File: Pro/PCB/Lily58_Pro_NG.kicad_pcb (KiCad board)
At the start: 2 copper layers, 142.5 x 106.3 mm, 87 parts, among them J1 LED, J2 4PIN, J3 OLED, P1 i2c_pin, P2 i2c_pin, SW1 SW_PUSH, SW10 SW_PUSH, SW11 SW_PUSH, SW12 SW_PUSH, SW13 SW_PUSH, SW14 SW_PUSH, SW15 SW_PUSH, SW16 SW_PUSH, SW17 SW_PUSH, SW18 SW_PUSH, SW19 SW_PUSH, SW2 SW_PUSH, SW20 SW_PUSH, SW21 SW_PUSH, SW22 SW_PUSH, SW23 SW_PUSH, SW24 SW_PUSH, SW25 SW_PUSH, SW26 SW_PUSH, SW27 SW_PUSH, SW28 SW_PUSH, SW29 SW_PUSH, SW3 SW_PUSH, SW30 SW_PUSH, SW31 Rotary_Encoder_Switch, SW4 SW_PUSH, SW5 SW_PUSH, SW6 SW_PUSH, SW7 SW_PUSH, SW8 SW_PUSH, SW9 SW_PUSH, U1 ProMicro

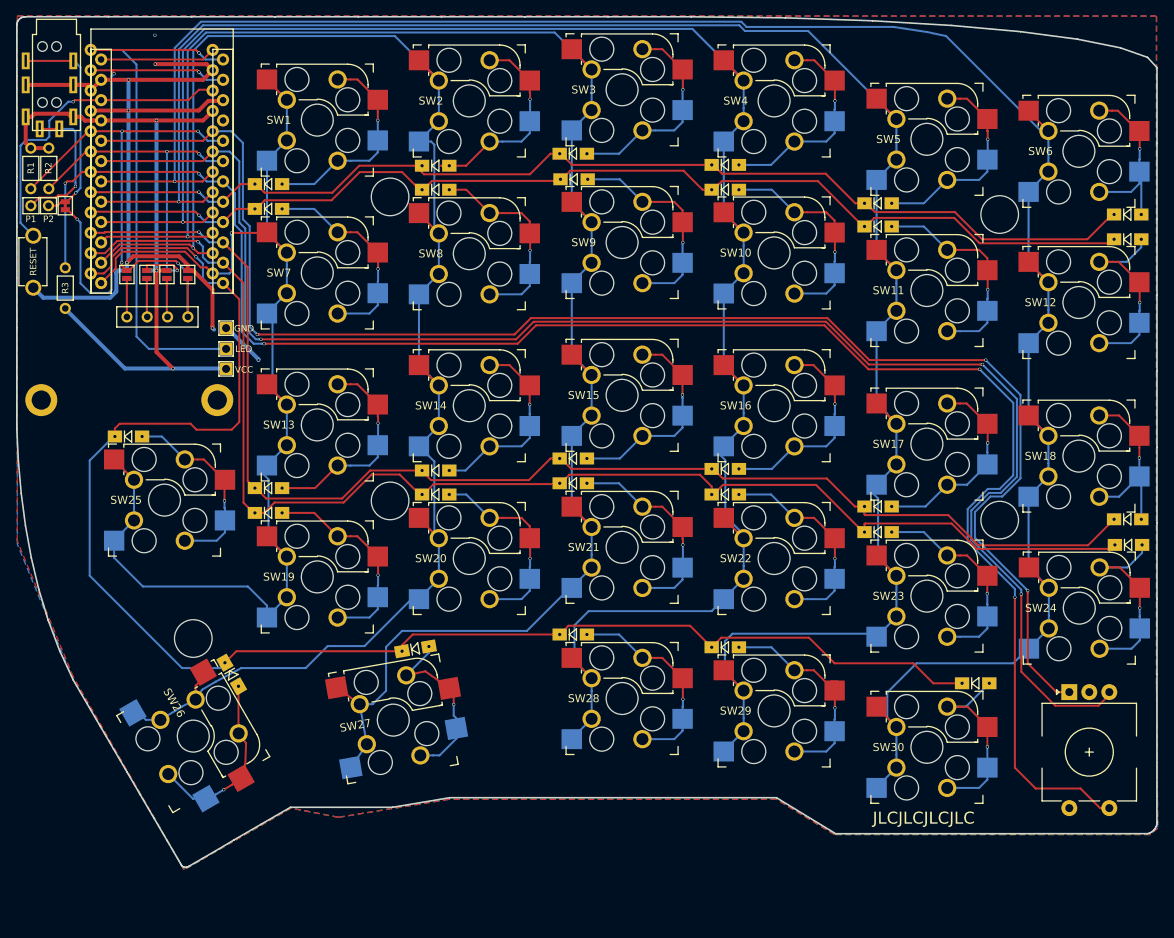
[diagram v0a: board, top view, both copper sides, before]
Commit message: Final version of Lily60 Evo PCB and Case
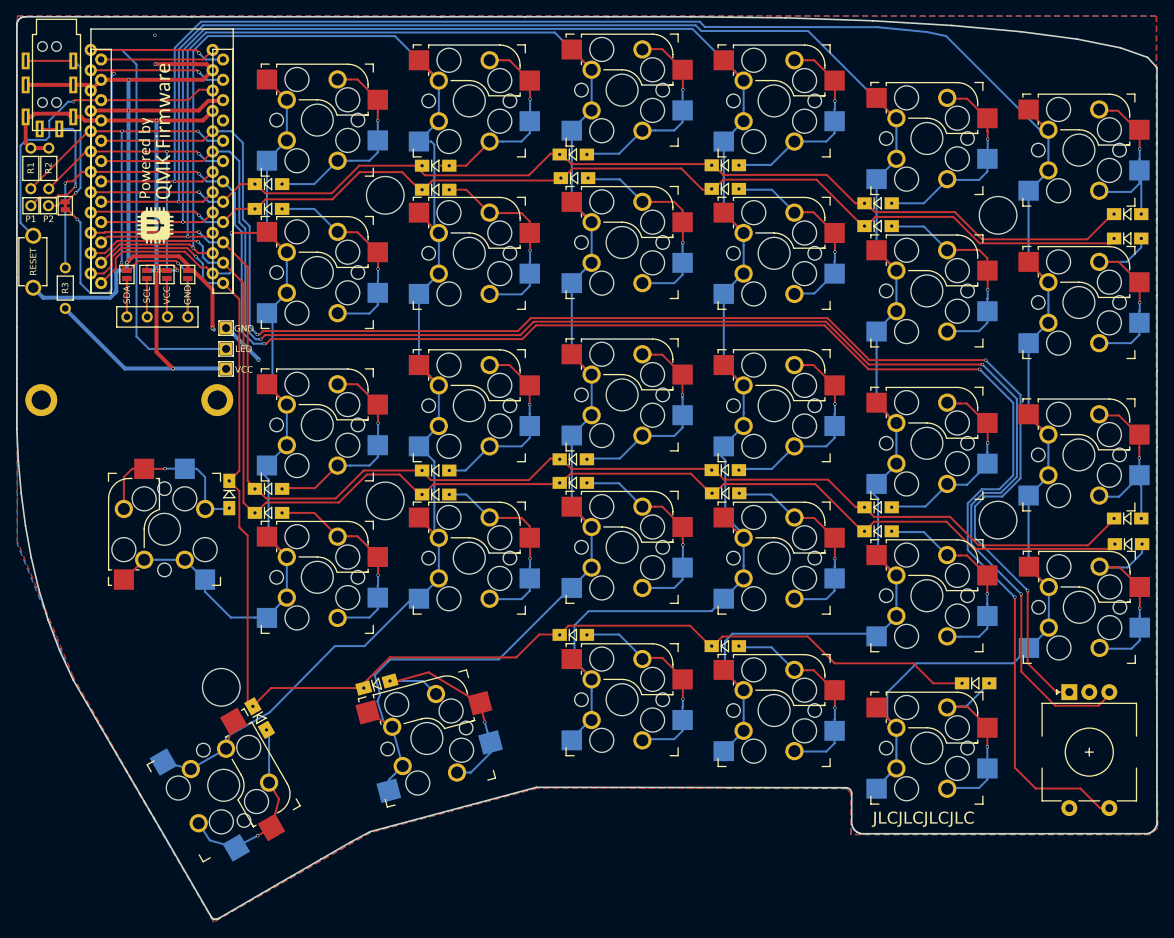
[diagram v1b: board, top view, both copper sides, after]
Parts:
- added G***: LOGO, Lily58_Pro-footprint:qmk-badge, B.Cu at (100.2, 54.1)
- added G***: LOGO, Lily58_Pro-footprint:qmk-badge, F.Cu at (100.2, 54.1)
- SW1, SW10, SW11, SW12, SW13, SW14, SW15, SW16, SW17, SW18, SW19, SW2, SW20, SW21, SW22, SW23, SW24, SW25, SW26, SW27, SW28, SW29, SW3, SW30, SW4, SW5, SW6, SW7, SW8, SW9: moved to B.Cu
- moved D25 14.5 mm to (109.5, 96.8), turned to 270 degrees
- moved SW26 7.23 mm to (108.8, 133.2)
- moved TH7 7.03 mm to (108.5, 120.9)
- moved D27 6.57 mm to (128.0, 120.5), turned to 15 degrees
- moved D26 6.48 mm to (113.3, 124.8)
- moved SW27 4.86 mm to (134.2, 127.3), turned to 15 degrees
- moved SW25 3.65 mm to (101.4, 101.2), turned to 90 degrees
- moved TH3 0.63 mm to (129.0, 59.4)
- moved TH5 0.60 mm to (129.0, 97.6)
- moved TH4 0.22 mm to (205.6, 61.9)
- moved TH6 0.20 mm to (205.6, 100.0)
- moved D9 0.16 mm to (152.7, 57.2)
- moved D22 0.16 mm to (171.6, 96.7)
- moved D16 0.15 mm to (171.5, 93.8)
- moved D29 0.15 mm to (171.5, 115.8)
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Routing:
- net row4: track 196.4 -> 174.2 mm
- net col5: track 155.0 -> 140.4 mm
- net Net-(D27-Pad2): track 22.9 -> 30.5 mm
- net Net-(D25-Pad2): track 26.2 -> 22.1 mm
- net Net-(D10-Pad2): track 28.7 -> 26.9 mm
- net col4: track 207.2 -> 205.6 mm
- net col3: track 225.3 -> 226.4 mm
- net row3: track 170.5 -> 169.8 mm
- net row2: track 167.0 -> 166.4 mm
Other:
- board size 142.5 x 106.3 mm -> 142.5 x 112.8 mm
- board text added: "GND"
- board text added: "SCL"
- board text added: "SDA"
- board text added: "VCC"

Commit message: SW31 can be an encoder or a MW Switch
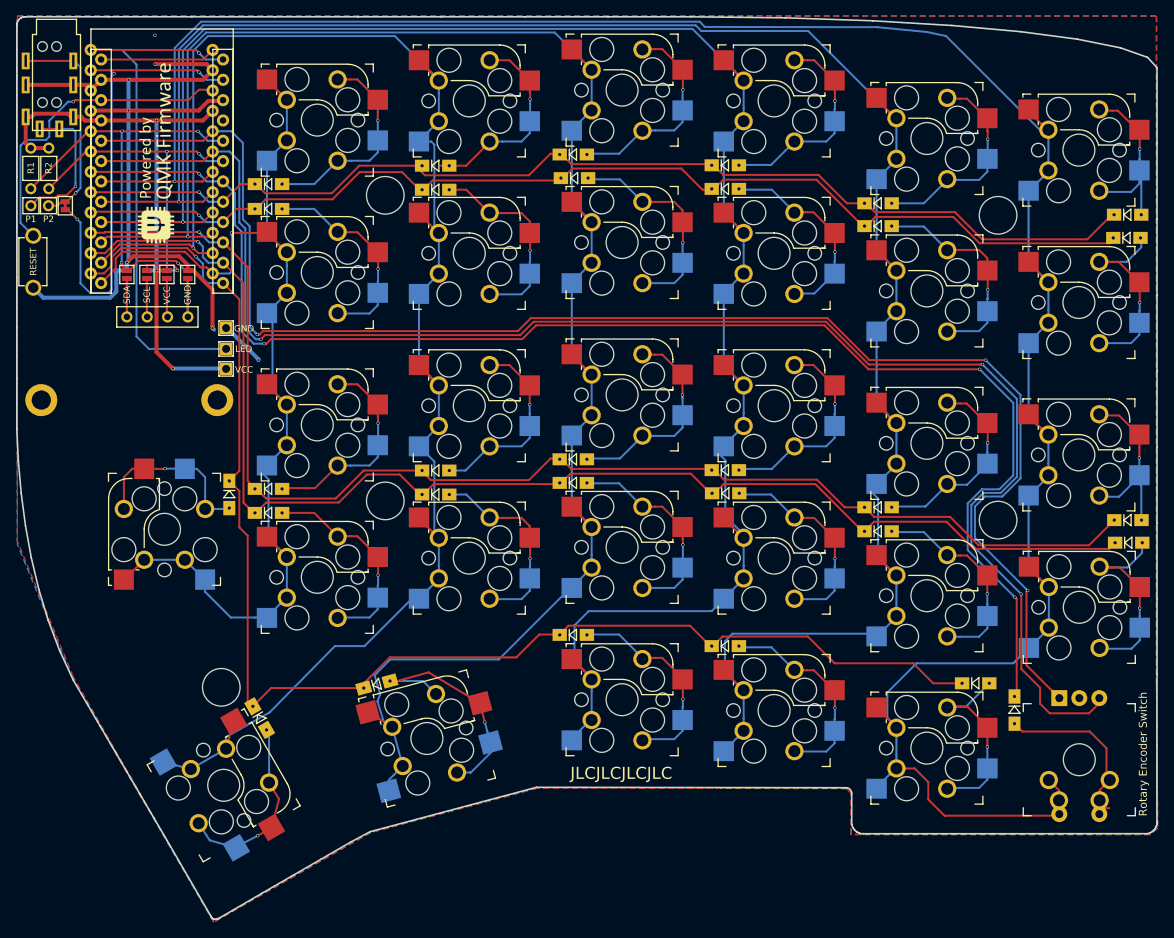
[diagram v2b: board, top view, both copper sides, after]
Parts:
- removed the G*** at (100.2, 54.1) (x2)
- removed R3: R, Lily58_Pro-footprint:RESISTOR_mini
- added D31: D, Lily58_Pro-footprint:Diode_SOD123, F.Cu at (207.7, 123.8)
- added G***: LOGO, Lily58_Pro-footprint:qmk-badge, B.Cu at (100.3, 54.1)
- added G***: LOGO, Lily58_Pro-footprint:qmk-badge, F.Cu at (100.3, 54.1)
- R1, R2: value R -> 4.7k
- SW31: value Rotary_Encoder_Switch -> Rotary Encoder Switch; footprint Keebio-parts:RotaryEncoder_EC11 -> Lily58_Pro-footprint:SW_MX_Reveresible_RotaryEncoder_EC11
- moved SW31 1.57 mm to (215.8, 129.9), turned to 0 degrees
- moved D18 0.20 mm to (221.8, 100.0)
- moved D24 0.18 mm to (221.9, 102.8)
- moved D12 0.13 mm to (221.7, 64.7)
- moved D6 0.08 mm to (221.8, 61.8)
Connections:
- U1 pad 7: SW31 -> row5
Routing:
- net SW31: track 218.7 -> 0.00 mm, vias 5 -> 0
- net row5: track 0.00 -> 181.8 mm, vias 0 -> 4
- net col0: track 270.3 -> 299.4 mm
- net Net-(D31-Pad2): track 0.00 -> 23.1 mm
- net VCC: track 88.4 -> 71.8 mm
